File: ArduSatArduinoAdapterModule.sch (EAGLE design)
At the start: 28 parts, among them J1 Power, J2 Analog, J3 D8_13, J4 D0_7, J5 M17, J6 M17, U1 ICSP, U2 ICSP-Breakout

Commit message: Switched to 4 layer PCB; completed all routing
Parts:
- removed U$2, U$5, U$6: (no value), freetronics-original:M06SIP
- removed U1: ICSP, freetronics-jon:ICSPPTH
- removed U2: ICSP-Breakout, freetronics-jon:ICSPPTH
- added SL10: (no value), freetronics-master-v1.1:M04PTH
- added SL11: (no value), freetronics-master-v1.1:M03PTH
- added SL12, SL8, SL9: (no value), freetronics-master-v1.1:M02PTH
- added SL13: (no value), freetronics-master-v1.1:M05PTH
- added SL5: ICSP-Breakout, freetronics-jon:ICSPPTH
- added SL6: M17, freetronics-master-v1.1:M17
- J5: value M17 -> ICSP; device freetronics-master-v1.1:M17 -> freetronics-jon:ICSPPTH
- LED1: value JADEGREEN 0603 -> BLUE 0603
- LED2: value BLUE 0603 -> JADEGREEN 0603
- R1: value 2K2 -> 2K2 0603
- R2: value 1K -> 1K 0603
- SL14: value CUBESATBUSH -> H1BREAKOUT
- SL15: value CUBESATBUSH -> H2BREAKOUT
- renumbered H1BREAKOUT to SL14, H2BREAKOUT to SL15, J6 to SL7
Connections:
- net +5V_SYS: now also SL11.1, SL11.2, SL11.3, SL8.1, SL8.2; no longer U$2.1, U$2.2, U$2.3, U$2.4, U$2.5, U$2.6
- net 5V: now also SL5.2, SL6.1, SL6.10, SL6.11, SL6.12, SL6.13, SL6.14, SL6.15, SL6.16, SL6.17, SL6.2, SL6.3, SL6.4, SL6.5, SL6.6, SL6.7, SL6.8, SL6.9; no longer J5.1, J5.10, J5.11, J5.12, J5.13, J5.14, J5.15, J5.16, J5.17, J5.3, J5.4, J5.5, J5.6, J5.7, J5.8, J5.9, U1.2, U2.2
- net GND: now also J5.6, SL10.1, SL10.2, SL10.3, SL10.4, SL13.1, SL13.2, SL13.3, SL13.4, SL13.5, SL5.6; no longer U$6.1, U$6.2, U$6.3, U$6.4, U$6.5, U$6.6, U1.6, U2.6
- net N$1: now also LED2.A; no longer LED1.A
- net N$35: now also J5.4, SL5.4; no longer U1.4, U2.4
- net N$51: now also J5.1, SL5.1; no longer U1.1, U2.1
- net N$52: now also J5.3, SL5.3; no longer U1.3, U2.3
- net N$53: now also J5.5, SL5.5; no longer U1.5, U2.5
- net N$6: now also LED1.A; no longer LED2.A
- net VCC_SYS: now also SL12.1, SL12.2, SL9.1, SL9.2; no longer U$5.1, U$5.2, U$5.3, U$5.4, U$5.5, U$5.6
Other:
- note added: "Arduino Header Breakout"
- note added: "ICSP Breakout"
- note added: "V1.0 (2012-12-19)"
- note removed: "Arduino Breakout"
- note removed: "Move power bus link to top. AS 5V and 3V3 rails top and bottom."
- note removed: "V1.0 (2012-12-10)"
- moved on the sheet: C1, C2, JP1, JP2, LED1, LED2, R1, R2, S1

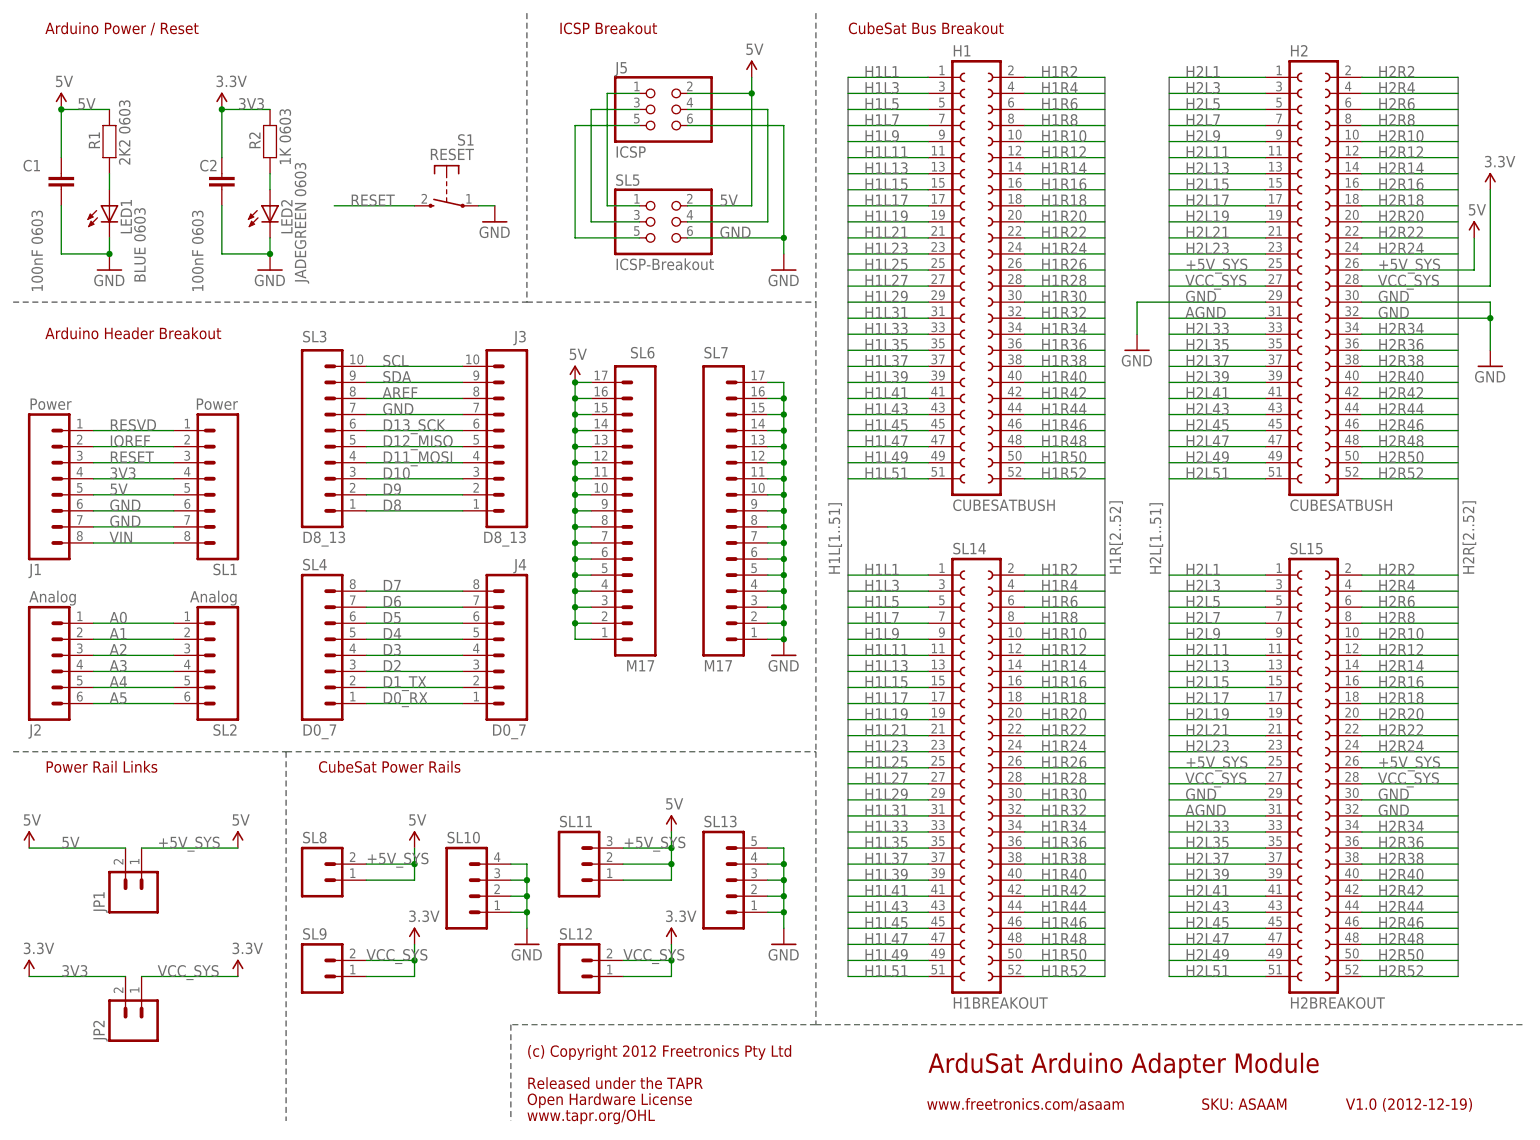
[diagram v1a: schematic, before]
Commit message: Added grounded corner mount holes and relocated some traces to inner layers to minimise risk of shorts to mounting sleeves
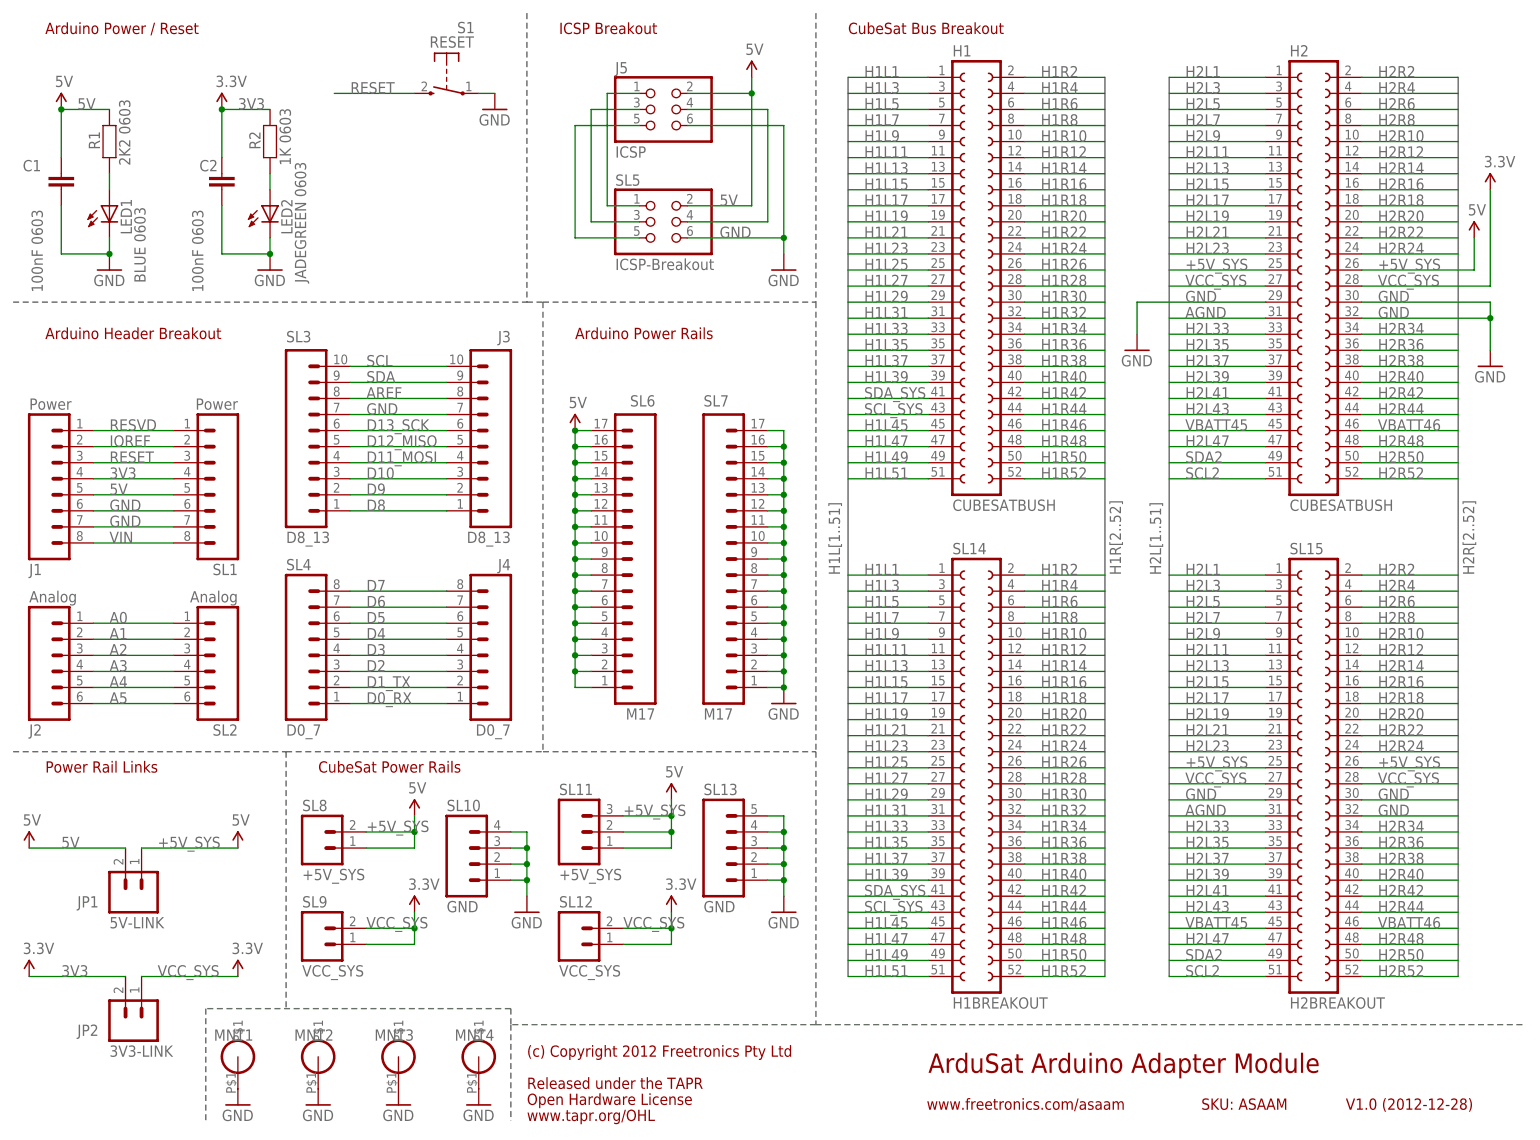
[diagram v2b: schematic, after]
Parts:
- added MNT1, MNT2, MNT3, MNT4: HOLE3.2MM, freetronics-jon:HOLE3.2MM
- JP1: value (none) -> 5V-LINK
- JP2: value (none) -> 3V3-LINK
- SL10, SL13: value (none) -> GND
- SL11, SL8: value (none) -> +5V_SYS
- SL12, SL9: value (none) -> VCC_SYS
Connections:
- net H1L41 renamed SDA_SYS
- net H1L43 renamed SCL_SYS
- net H2L45 renamed VBATT45
- net H2L49 renamed SDA2
- net H2L51 renamed SCL2
- net H2R46 renamed VBATT46
- net GND: now also MNT1.P$1, MNT2.P$1, MNT3.P$1, MNT4.P$1
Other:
- note added: "Arduino Power Rails"
- note added: "V1.0 (2012-12-28)"
- note removed: "V1.0 (2012-12-19)"
- moved on the sheet: J3, J4, S1, SL10, SL11, SL12, SL13, SL3, SL4, SL6, SL7, SL8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
